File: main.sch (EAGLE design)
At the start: 474 parts, among them J100 DCJ0202, Q200 NMOS, Q201 PMOS, Q300 PMOS, Q400 PMOS, U100 NE555N, U1000 74LS173N, U1001 74LS173N, U1002 74LS245N, U1003 74LS173N, U1004 74LS173N, U1005 74LS245N, U101 NE555N, U102 NE555N, U103 74LS04N, U104 74LS08N, U105 74LS32N, U1100 74LS173N, U1101 74LS173N, U1102 74LS161N, U1106 74HCT154DW, U1107 74HCT154DW, U1108 74LS04N, U1109 74LS04N, U200 HM62256, U201 74LS173N, U202 74LS173N, U203 74LS173N, U204 74LS173N, U205 74LS157N, U206 74LS157N, U207 74LS157N, U208 74LS157N, U209 74HCT595D, U210 74HCT595D, U211 74HCT595D, U212 74LS245N, U213 74LS245N, U214 74LS00N, U215 74LS173N, U216 74LS173N, U217 74LS173N, U218 74LS173N, U219 74LS245N, U220 74LS245N, U300 74LS299N, U301 74LS245N, U302 74LS08N, U303 74LS00N, U304 74LS245N, U400 74LS00N, U401 74LS245N, U500 74LS161N, U501 74LS161N, U502 74LS161N, U503 74LS161N, U504 74LS245N, U505 74LS245N, U600 74LS173N, U601 74LS173N, U602 74LS173N, U603 74LS173N, U604 74LS245N, U700 74LS283N, U701 74LS283N, U702 74LS245N, U703 74LS86N, U704 74LS86N, U705 74LS85N, U706 74LS85N, U707 74LS173N, U708 74LS125N, U800 74LS04N, U801 74LS04N, U802 74LS08N, U803 74LS08N, U804 74LS32N, U805 74LS32N, U806 74LS86N, U807 74LS86N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

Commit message: Moved ResNet to included library.
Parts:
- RN1000, RN1001, RN1100, RN1101, RN1102, RN1103, RN1104, RN1105, RN1106, RN1107, RN200, RN201, RN202, RN203, RN204, RN205, RN206, RN207, RN300, RN301, RN302, RN400, RN500, RN501, RN600, RN601, RN700, RN800, RN900: device SamacSys_Parts:CAY16-102J8LF -> 8BitCpuParts:CAY16-102J8LF

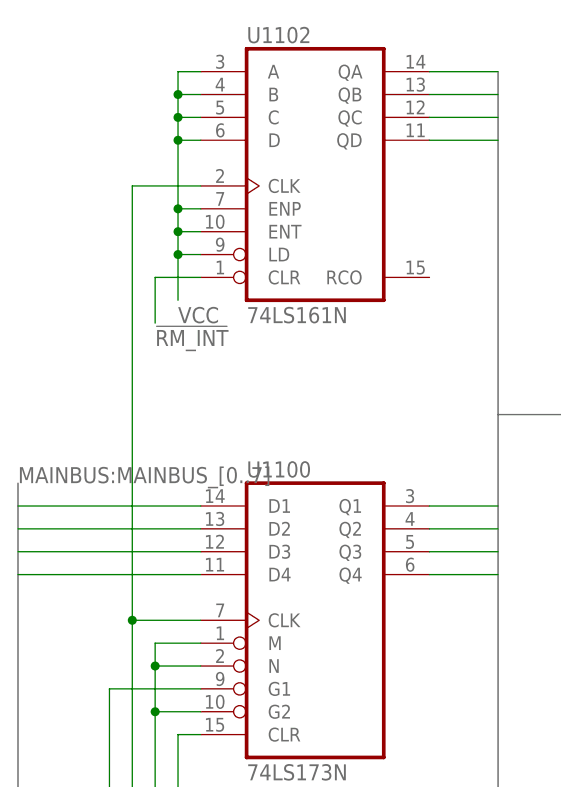
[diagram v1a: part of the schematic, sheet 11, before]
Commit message: Most inter-module connections done, added RESET.
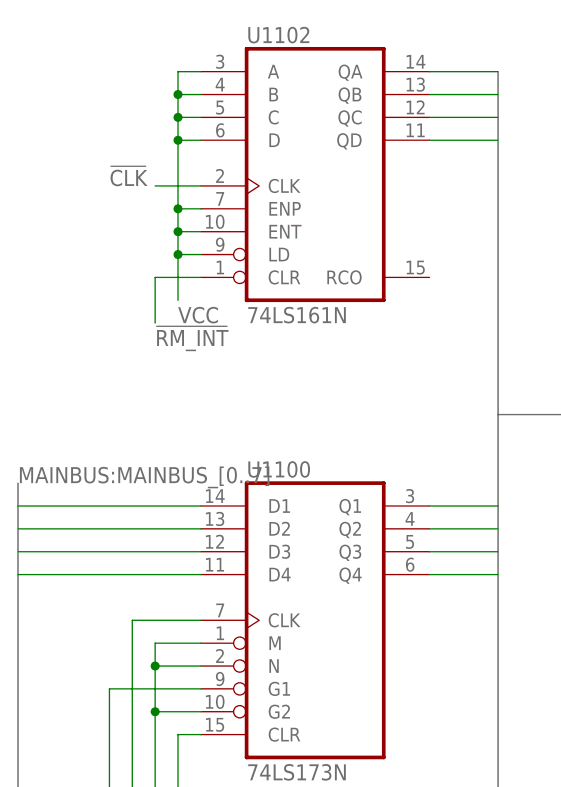
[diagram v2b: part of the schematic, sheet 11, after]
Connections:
- new net !CLK: U1102G$1.CLK
- net CLK: no longer U1102G$1.CLK
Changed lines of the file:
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@@
 <?xml version="1.0" encoding="utf-8"?>
 <!DOCTYPE eagle SYSTEM "eagle.dtd">
-<eagle version="9.3.1">
+<eagle version="9.3.2">
 <drawing>
 <settings>
@@
 <junction x="40.64" y="0"/>
 <label x="40.64" y="-22.86" size="1.778" layer="255"/>
-<pinref part="U1102" gate="G$1" pin="CLK"/>
-<wire x1="48.26" y1="86.36" x2="40.64" y2="86.36" width="0.1524" layer="91"/>
-<wire x1="40.64" y1="86.36" x2="40.64" y2="38.1" width="0.1524" layer="91"/>
-<junction x="40.64" y="38.1"/>
 </segment>
 </net>
@@
 </segment>
 </net>
+<net name="!CLK" class="0">
+<segment>
+<pinref part="U1102" gate="G$1" pin="CLK"/>
+<wire x1="48.26" y1="86.36" x2="43.18" y2="86.36" width="0.1524" layer="91"/>
+<label x="38.1" y="86.36" size="1.778" layer="95"/>
+</segment>
+</net>

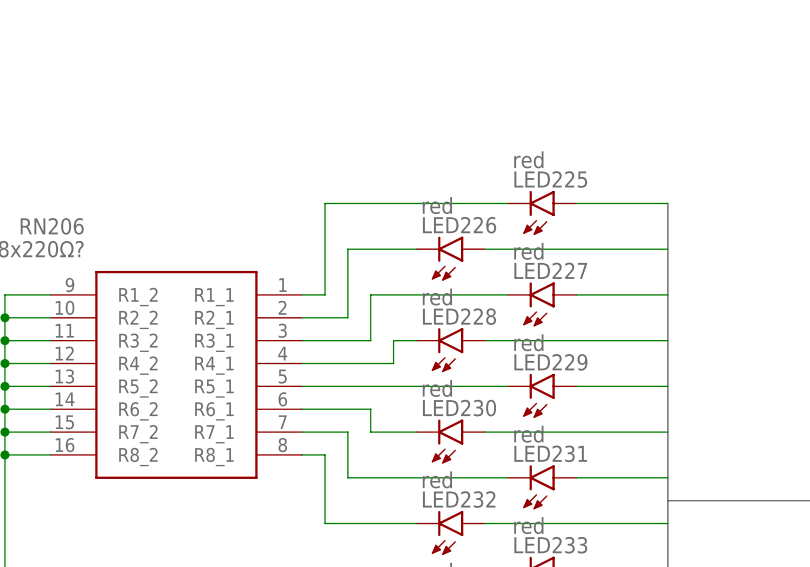
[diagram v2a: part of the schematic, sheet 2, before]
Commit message: Z register mostly done.
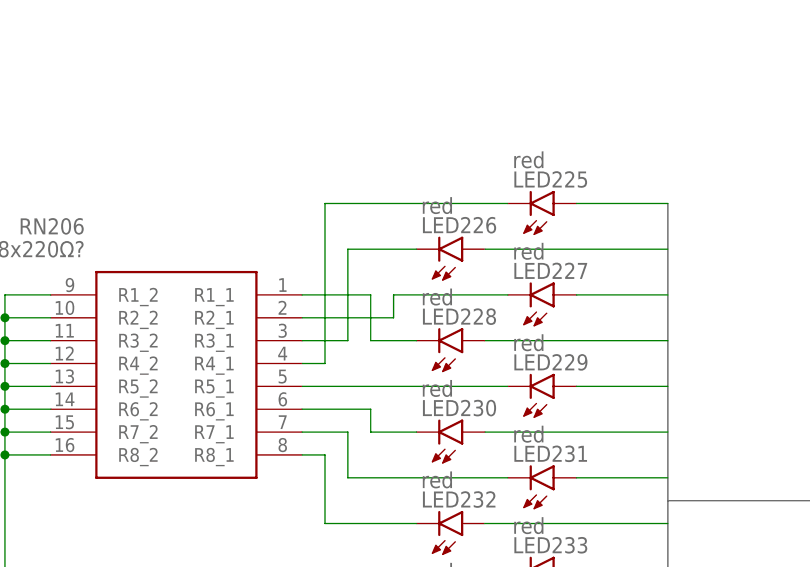
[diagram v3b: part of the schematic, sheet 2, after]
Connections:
- net LED225_GND: now also RN206.R4_1; no longer RN206.R1_1
- net LED226_GND: now also RN206.R3_1; no longer RN206.R2_1
- net LED227_GND: now also RN206.R2_1; no longer RN206.R3_1
- net LED228_GND: now also RN206.R1_1; no longer RN206.R4_1
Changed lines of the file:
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@@
 <?xml version="1.0" encoding="utf-8"?>
 <!DOCTYPE eagle SYSTEM "eagle.dtd">
-<eagle version="9.3.2">
+<eagle version="9.4.0">
 <drawing>
 <settings>
@@
 <pinref part="LED225" gate="G$1" pin="C"/>
 <wire x1="-195.58" y1="-58.42" x2="-215.9" y2="-58.42" width="0.1524" layer="91"/>
-<wire x1="-215.9" y1="-58.42" x2="-215.9" y2="-68.58" width="0.1524" layer="91"/>
-<pinref part="RN206" gate="G$1" pin="R1_1"/>
-<wire x1="-215.9" y1="-68.58" x2="-218.44" y2="-68.58" width="0.1524" layer="91"/>
+<wire x1="-215.9" y1="-58.42" x2="-215.9" y2="-76.2" width="0.1524" layer="91"/>
+<pinref part="RN206" gate="G$1" pin="R4_1"/>
+<wire x1="-215.9" y1="-76.2" x2="-218.44" y2="-76.2" width="0.1524" layer="91"/>
 </segment>
 </net>
@@
 <pinref part="LED226" gate="G$1" pin="C"/>
 <wire x1="-205.74" y1="-63.5" x2="-213.36" y2="-63.5" width="0.1524" layer="91"/>
-<wire x1="-213.36" y1="-63.5" x2="-213.36" y2="-71.12" width="0.1524" layer="91"/>
-<pinref part="RN206" gate="G$1" pin="R2_1"/>
-<wire x1="-213.36" y1="-71.12" x2="-218.44" y2="-71.12" width="0.1524" layer="91"/>
+<wire x1="-213.36" y1="-63.5" x2="-213.36" y2="-73.66" width="0.1524" layer="91"/>
+<pinref part="RN206" gate="G$1" pin="R3_1"/>
+<wire x1="-213.36" y1="-73.66" x2="-218.44" y2="-73.66" width="0.1524" layer="91"/>
 </segment>
 </net>
@@
 <segment>
 <pinref part="LED227" gate="G$1" pin="C"/>
-<wire x1="-195.58" y1="-68.58" x2="-210.82" y2="-68.58" width="0.1524" layer="91"/>
-<wire x1="-210.82" y1="-68.58" x2="-210.82" y2="-73.66" width="0.1524" layer="91"/>
-<pinref part="RN206" gate="G$1" pin="R3_1"/>
-<wire x1="-210.82" y1="-73.66" x2="-218.44" y2="-73.66" width="0.1524" layer="91"/>
+<wire x1="-195.58" y1="-68.58" x2="-208.28" y2="-68.58" width="0.1524" layer="91"/>
+<wire x1="-208.28" y1="-68.58" x2="-208.28" y2="-71.12" width="0.1524" layer="91"/>
+<pinref part="RN206" gate="G$1" pin="R2_1"/>
+<wire x1="-208.28" y1="-71.12" x2="-218.44" y2="-71.12" width="0.1524" layer="91"/>
 </segment>
 </net>
@@
 <segment>
 <pinref part="LED228" gate="G$1" pin="C"/>
-<wire x1="-205.74" y1="-73.66" x2="-208.28" y2="-73.66" width="0.1524" layer="91"/>
-<wire x1="-208.28" y1="-73.66" x2="-208.28" y2="-76.2" width="0.1524" layer="91"/>
-<pinref part="RN206" gate="G$1" pin="R4_1"/>
-<wire x1="-208.28" y1="-76.2" x2="-218.44" y2="-76.2" width="0.1524" layer="91"/>
+<wire x1="-205.74" y1="-73.66" x2="-210.82" y2="-73.66" width="0.1524" layer="91"/>
+<wire x1="-210.82" y1="-73.66" x2="-210.82" y2="-68.58" width="0.1524" layer="91"/>
+<pinref part="RN206" gate="G$1" pin="R1_1"/>
+<wire x1="-210.82" y1="-68.58" x2="-218.44" y2="-68.58" width="0.1524" layer="91"/>
 </segment>
 </net>

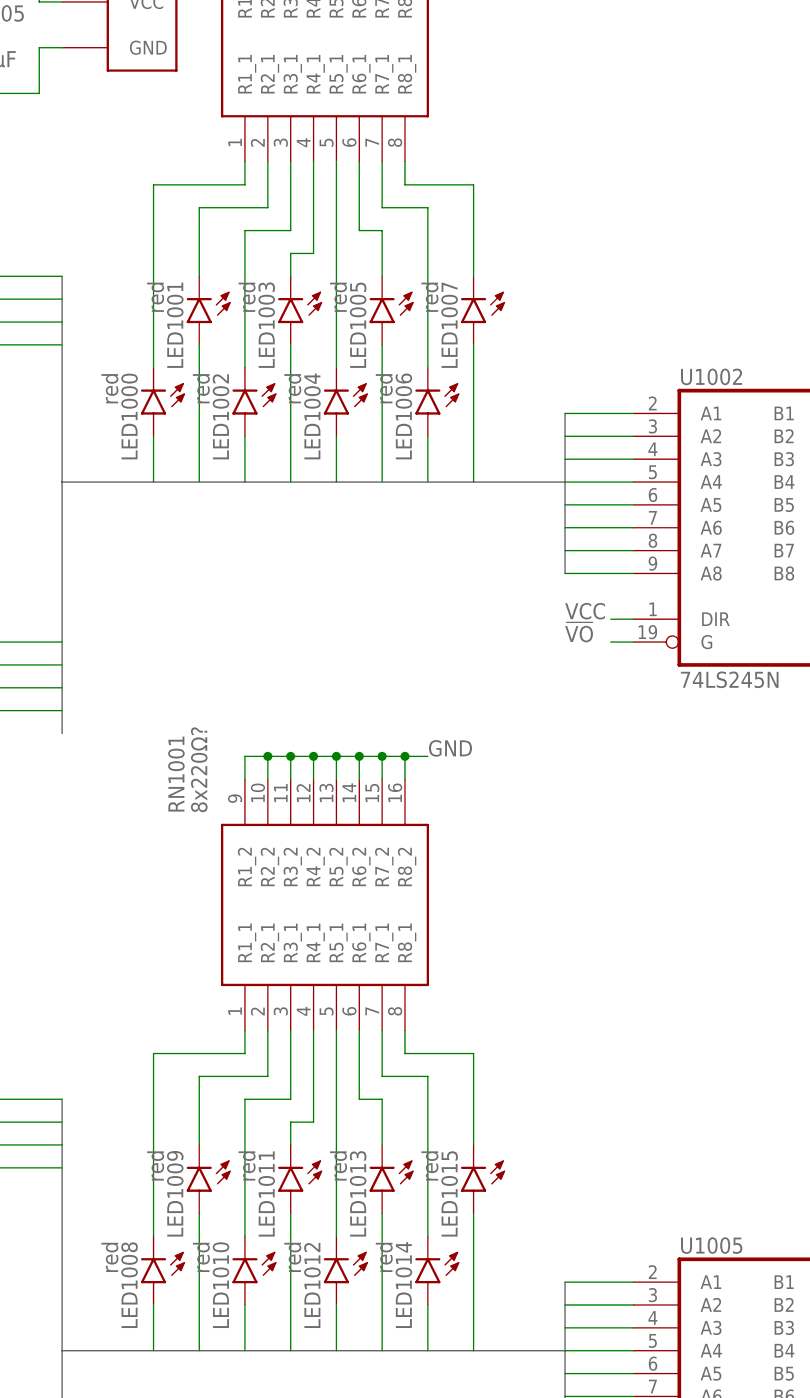
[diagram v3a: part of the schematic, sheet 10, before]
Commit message: Finished Z, V and F registers.
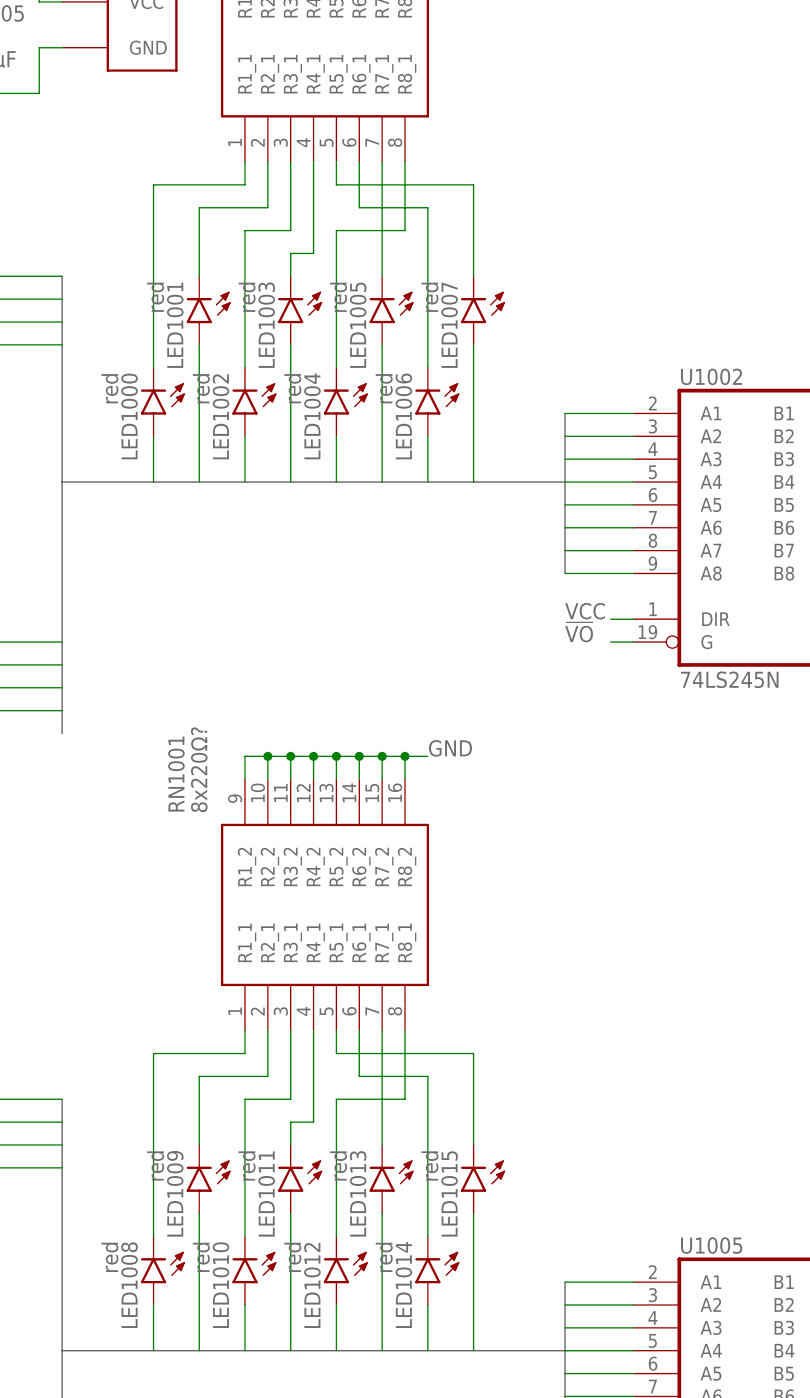
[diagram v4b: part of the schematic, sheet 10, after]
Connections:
- net LED1004_GND: now also RN1000.R8_1; no longer RN1000.R5_1
- net LED1005_GND: now also RN1000.R7_1; no longer RN1000.R6_1
- net LED1006_GND: now also RN1000.R6_1; no longer RN1000.R7_1
- net LED1007_GND: now also RN1000.R5_1; no longer RN1000.R8_1
- net LED1012_GND: now also RN1001.R8_1; no longer RN1001.R5_1
- net LED1013_GND: now also RN1001.R7_1; no longer RN1001.R6_1
- net LED1014_GND: now also RN1001.R6_1; no longer RN1001.R7_1
- net LED1015_GND: now also RN1001.R5_1; no longer RN1001.R8_1
- net LED237_GND: now also RN207.R8_1; no longer RN207.R5_1
- net LED238_GND: now also RN207.R7_1; no longer RN207.R6_1
- net LED239_GND: now also RN207.R6_1; no longer RN207.R7_1
- net LED240_GND: now also RN207.R5_1; no longer RN207.R8_1
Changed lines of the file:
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@@
 </segment>
 </net>
-<net name="LED236_GND" class="0">
-<segment>
-<pinref part="LED236" gate="G$1" pin="C"/>
-<wire x1="-205.74" y1="-114.3" x2="-208.28" y2="-114.3" width="0.1524" layer="91"/>
-<wire x1="-208.28" y1="-114.3" x2="-208.28" y2="-116.84" width="0.1524" layer="91"/>
-<pinref part="RN207" gate="G$1" pin="R4_1"/>
-<wire x1="-208.28" y1="-116.84" x2="-218.44" y2="-116.84" width="0.1524" layer="91"/>
-</segment>
-</net>
-<net name="LED237_GND" class="0">
-<segment>
-<pinref part="LED237" gate="G$1" pin="C"/>
-<pinref part="RN207" gate="G$1" pin="R5_1"/>
-<wire x1="-195.58" y1="-119.38" x2="-218.44" y2="-119.38" width="0.1524" layer="91"/>
-</segment>
-</net>
 <net name="LED239_GND" class="0">
 <segment>
 <pinref part="LED239" gate="G$1" pin="C"/>
 <wire x1="-195.58" y1="-129.54" x2="-213.36" y2="-129.54" width="0.1524" layer="91"/>
-<wire x1="-213.36" y1="-129.54" x2="-213.36" y2="-124.46" width="0.1524" layer="91"/>
-<pinref part="RN207" gate="G$1" pin="R7_1"/>
-<wire x1="-213.36" y1="-124.46" x2="-218.44" y2="-124.46" width="0.1524" layer="91"/>
+<wire x1="-213.36" y1="-129.54" x2="-213.36" y2="-121.92" width="0.1524" layer="91"/>
+<pinref part="RN207" gate="G$1" pin="R6_1"/>
+<wire x1="-213.36" y1="-121.92" x2="-218.44" y2="-121.92" width="0.1524" layer="91"/>
 </segment>
 </net>
@@
 <segment>
 <pinref part="LED238" gate="G$1" pin="C"/>
-<wire x1="-205.74" y1="-124.46" x2="-210.82" y2="-124.46" width="0.1524" layer="91"/>
-<wire x1="-210.82" y1="-124.46" x2="-210.82" y2="-121.92" width="0.1524" layer="91"/>
-<pinref part="RN207" gate="G$1" pin="R6_1"/>
-<wire x1="-210.82" y1="-121.92" x2="-218.44" y2="-121.92" width="0.1524" layer="91"/>
+<pinref part="RN207" gate="G$1" pin="R7_1"/>
+<wire x1="-205.74" y1="-124.46" x2="-218.44" y2="-124.46" width="0.1524" layer="91"/>
 </segment>
 </net>
 <net name="LED240_GND" class="0">
 <segment>
-<pinref part="RN207" gate="G$1" pin="R8_1"/>
-<wire x1="-218.44" y1="-127" x2="-215.9" y2="-127" width="0.1524" layer="91"/>
 <pinref part="LED240" gate="G$1" pin="C"/>
-<wire x1="-215.9" y1="-127" x2="-215.9" y2="-134.62" width="0.1524" layer="91"/>
 <wire x1="-215.9" y1="-134.62" x2="-205.74" y2="-134.62" width="0.1524" layer="91"/>
+<pinref part="RN207" gate="G$1" pin="R5_1"/>
+<wire x1="-218.44" y1="-119.38" x2="-215.9" y2="-119.38" width="0.1524" layer="91"/>
+<wire x1="-215.9" y1="-119.38" x2="-215.9" y2="-134.62" width="0.1524" layer="91"/>
 </segment>
 </net>
@@
 </segment>
 </net>
+<net name="LED236_GND" class="0">
+<segment>
+<pinref part="LED236" gate="G$1" pin="C"/>
+<wire x1="-205.74" y1="-114.3" x2="-208.28" y2="-114.3" width="0.1524" layer="91"/>
+<wire x1="-208.28" y1="-114.3" x2="-208.28" y2="-116.84" width="0.1524" layer="91"/>
+<pinref part="RN207" gate="G$1" pin="R4_1"/>
+<wire x1="-208.28" y1="-116.84" x2="-218.44" y2="-116.84" width="0.1524" layer="91"/>
+</segment>
+</net>
+<net name="LED237_GND" class="0">
+<segment>
+<pinref part="LED237" gate="G$1" pin="C"/>
+<wire x1="-195.58" y1="-119.38" x2="-210.82" y2="-119.38" width="0.1524" layer="91"/>
+<wire x1="-210.82" y1="-119.38" x2="-210.82" y2="-127" width="0.1524" layer="91"/>
+<pinref part="RN207" gate="G$1" pin="R8_1"/>
+<wire x1="-210.82" y1="-127" x2="-218.44" y2="-127" width="0.1524" layer="91"/>
+</segment>
+</net>
 </nets>
 </sheet>
@@
 <pinref part="LED1007" gate="G$1" pin="C"/>
 <wire x1="55.88" y1="104.14" x2="55.88" y2="114.3" width="0.1524" layer="91"/>
-<wire x1="55.88" y1="114.3" x2="48.26" y2="114.3" width="0.1524" layer="91"/>
-<pinref part="RN1000" gate="G$1" pin="R8_1"/>
-<wire x1="48.26" y1="114.3" x2="48.26" y2="116.84" width="0.1524" layer="91"/>
+<wire x1="55.88" y1="114.3" x2="40.64" y2="114.3" width="0.1524" layer="91"/>
+<pinref part="RN1000" gate="G$1" pin="R5_1"/>
+<wire x1="40.64" y1="114.3" x2="40.64" y2="116.84" width="0.1524" layer="91"/>
 </segment>
 </net>
@@
 </segment>
 </net>
-<net name="LED1004_GND" class="0">
-<segment>
-<pinref part="LED1004" gate="G$1" pin="C"/>
-<pinref part="RN1000" gate="G$1" pin="R5_1"/>
-<wire x1="40.64" y1="93.98" x2="40.64" y2="116.84" width="0.1524" layer="91"/>
-</segment>
-</net>
 <net name="LED1006_GND" class="0">
 <segment>
 <pinref part="LED1006" gate="G$1" pin="C"/>
 <wire x1="50.8" y1="93.98" x2="50.8" y2="111.76" width="0.1524" layer="91"/>
-<wire x1="50.8" y1="111.76" x2="45.72" y2="111.76" width="0.1524" layer="91"/>
-<pinref part="RN1000" gate="G$1" pin="R7_1"/>
-<wire x1="45.72" y1="111.76" x2="45.72" y2="116.84" width="0.1524" layer="91"/>
+<wire x1="50.8" y1="111.76" x2="43.18" y2="111.76" width="0.1524" layer="91"/>
+<pinref part="RN1000" gate="G$1" pin="R6_1"/>
+<wire x1="43.18" y1="111.76" x2="43.18" y2="116.84" width="0.1524" layer="91"/>
 </segment>
 </net>
@@
 <segment>
 <pinref part="LED1005" gate="G$1" pin="C"/>
-<wire x1="45.72" y1="104.14" x2="45.72" y2="109.22" width="0.1524" layer="91"/>
-<wire x1="45.72" y1="109.22" x2="43.18" y2="109.22" width="0.1524" layer="91"/>
-<pinref part="RN1000" gate="G$1" pin="R6_1"/>
-<wire x1="43.18" y1="109.22" x2="43.18" y2="116.84" width="0.1524" layer="91"/>
+<pinref part="RN1000" gate="G$1" pin="R7_1"/>
+<wire x1="45.72" y1="104.14" x2="45.72" y2="116.84" width="0.1524" layer="91"/>
 </segment>
 </net>
@@
 <pinref part="LED1015" gate="G$1" pin="C"/>
 <wire x1="55.88" y1="7.62" x2="55.88" y2="17.78" width="0.1524" layer="91"/>
-<wire x1="55.88" y1="17.78" x2="48.26" y2="17.78" width="0.1524" layer="91"/>
-<pinref part="RN1001" gate="G$1" pin="R8_1"/>
-<wire x1="48.26" y1="17.78" x2="48.26" y2="20.32" width="0.1524" layer="91"/>
+<wire x1="55.88" y1="17.78" x2="40.64" y2="17.78" width="0.1524" layer="91"/>
+<pinref part="RN1001" gate="G$1" pin="R5_1"/>
+<wire x1="40.64" y1="17.78" x2="40.64" y2="20.32" width="0.1524" layer="91"/>
 </segment>
 </net>
@@
 </segment>
 </net>
-<net name="LED1012_GND" class="0">
-<segment>
-<pinref part="LED1012" gate="G$1" pin="C"/>
-<pinref part="RN1001" gate="G$1" pin="R5_1"/>
-<wire x1="40.64" y1="-2.54" x2="40.64" y2="20.32" width="0.1524" layer="91"/>
-</segment>
-</net>
 <net name="LED1014_GND" class="0">
 <segment>
 <pinref part="LED1014" gate="G$1" pin="C"/>
 <wire x1="50.8" y1="-2.54" x2="50.8" y2="15.24" width="0.1524" layer="91"/>
-<wire x1="50.8" y1="15.24" x2="45.72" y2="15.24" width="0.1524" layer="91"/>
-<pinref part="RN1001" gate="G$1" pin="R7_1"/>
-<wire x1="45.72" y1="15.24" x2="45.72" y2="20.32" width="0.1524" layer="91"/>
+<wire x1="50.8" y1="15.24" x2="43.18" y2="15.24" width="0.1524" layer="91"/>
+<pinref part="RN1001" gate="G$1" pin="R6_1"/>
+<wire x1="43.18" y1="15.24" x2="43.18" y2="20.32" width="0.1524" layer="91"/>
 </segment>
 </net>
@@
 <segment>
 <pinref part="LED1013" gate="G$1" pin="C"/>
-<wire x1="45.72" y1="7.62" x2="45.72" y2="12.7" width="0.1524" layer="91"/>
-<wire x1="45.72" y1="12.7" x2="43.18" y2="12.7" width="0.1524" layer="91"/>
-<pinref part="RN1001" gate="G$1" pin="R6_1"/>
-<wire x1="43.18" y1="12.7" x2="43.18" y2="20.32" width="0.1524" layer="91"/>
+<pinref part="RN1001" gate="G$1" pin="R7_1"/>
+<wire x1="45.72" y1="20.32" x2="45.72" y2="7.62" width="0.1524" layer="91"/>
 </segment>
 </net>
@@
 </segment>
 </net>
+<net name="LED1004_GND" class="0">
+<segment>
+<pinref part="LED1004" gate="G$1" pin="C"/>
+<wire x1="40.64" y1="93.98" x2="40.64" y2="109.22" width="0.1524" layer="91"/>
+<wire x1="40.64" y1="109.22" x2="48.26" y2="109.22" width="0.1524" layer="91"/>
+<pinref part="RN1000" gate="G$1" pin="R8_1"/>
+<wire x1="48.26" y1="109.22" x2="48.26" y2="116.84" width="0.1524" layer="91"/>
+</segment>
+</net>
+<net name="LED1012_GND" class="0">
+<segment>
+<pinref part="LED1012" gate="G$1" pin="C"/>
+<wire x1="40.64" y1="-2.54" x2="40.64" y2="12.7" width="0.1524" layer="91"/>
+<wire x1="40.64" y1="12.7" x2="48.26" y2="12.7" width="0.1524" layer="91"/>
+<pinref part="RN1001" gate="G$1" pin="R8_1"/>
+<wire x1="48.26" y1="12.7" x2="48.26" y2="20.32" width="0.1524" layer="91"/>
+</segment>
+</net>
